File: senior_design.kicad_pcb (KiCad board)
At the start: 2 copper layers, 128.6 x 80.8 mm, 129 parts, among them J10 Conn_01x01_Pin, J11 Conn_01x01_Pin, J12 Conn_01x01_Pin, J13 Conn_ARM_JTAG_SWD_10, J2 Conn_01x03_Pin, J3 Conn_01x09_Socket, J4 USB_B_Micro, J5 Out_to_display, J6 AudioJack3, J7 SD_Card_Receptacle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

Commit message: Some fixes
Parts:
- removed C27: 1uF, Capacitor_SMD:C_0805_2012Metric
- C21, C22, L1, R41: moved to F.Cu
- C25, C26: value 0.1uF -> .1uF; moved to F.Cu
- C30, C8: moved to B.Cu
- C31: value 0.1uF -> 1uF; moved to B.Cu
- R38: value R -> 10k
- moved C31 36.9 mm to (231.6, 93.7), turned to 0 degrees
- moved C33 28.4 mm to (228.2, 77.5), turned to 90 degrees
- moved C28 26.9 mm to (207.2, 92.5), turned to 180 degrees
- moved C26 23.1 mm to (208.3, 97.0), turned to 180 degrees
- moved C34 15.5 mm to (218.1, 90.3), turned to 0 degrees
- moved C22 13.9 mm to (206.4, 81.7), turned to 0 degrees
- moved C32 12.9 mm to (229.4, 67.1), turned to 0 degrees
- moved R41 11.3 mm to (223.1, 66.2)
- moved C29 11.1 mm to (216.9, 87.7), turned to 0 degrees
- moved C30 10.8 mm to (218.0, 96.0), turned to 90 degrees
- moved C16 10.5 mm to (224.8, 56.5), turned to -90 degrees
- moved Y1 9.98 mm to (208.8, 78.2), turned to 0 degrees
- moved R38 9.40 mm to (208.8, 84.2), turned to 180 degrees
- moved D6 8.10 mm to (216.7, 79.7)
- moved L1 7.83 mm to (228.4, 62.0), turned to 90 degrees
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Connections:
- C23 pad 1: +1V5 -> CORE_VDD
- C24 pad 1: +1V5 -> CORE_VDD
- C25 pad 1: +1V5 -> +3.3V
- C26 pad 1: +1V5 -> +3.3V
- C30 pad 1: +3.3V -> GND
- C30 pad 2: GND -> CORE_VDD
- C31 pad 1: +3.3V -> CORE_VDD
- C34 pad 1: +3.3V -> Net-(U3-OSC_VDD)
- U3 pad 17: +1V5 -> CORE_VDD
- U3 pad 38: +1V5 -> CORE_VDD
- U3 pad 5: +1V5 -> Net-(U3-OSC_VDD)
- U3 pad 60: +1V5 -> CORE_VDD
- U3 pad 86: +1V5 -> CORE_VDD
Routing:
- net +1V5: track 56.3 -> 0.00 mm, vias 6 -> 0
- net CORE_VDD: track 0.00 -> 45.9 mm, vias 0 -> 6
- net GND: track 189.6 -> 218.0 mm, vias 73 -> 79
- net /Peripherals/X_0: track 24.3 -> 11.7 mm, vias 1 -> 0
- net Net-(D6-A): track 24.6 -> 13.9 mm, vias 0 -> 1
- net /Peripherals/X_1: track 20.1 -> 10.00 mm, vias 1 -> 0
- net Net-(U3-OSC_VDD): track 0.00 -> 6.78 mm, vias 0 -> 1
- net /Peripherals/LEDK: track 28.3 -> 34.5 mm
- net +3.3V: track 186.7 -> 181.6 mm
- net +5V: track 148.8 -> 152.4 mm, vias 4 -> 2
- net Net-(D7-A): track 14.6 -> 11.9 mm, vias 1 -> 0
- net /Peripherals/VSYNC: track 45.1 -> 43.8 mm
- net +24V: track 13.8 -> 14.7 mm
- net /Peripherals/PWM0: track 18.1 -> 17.6 mm

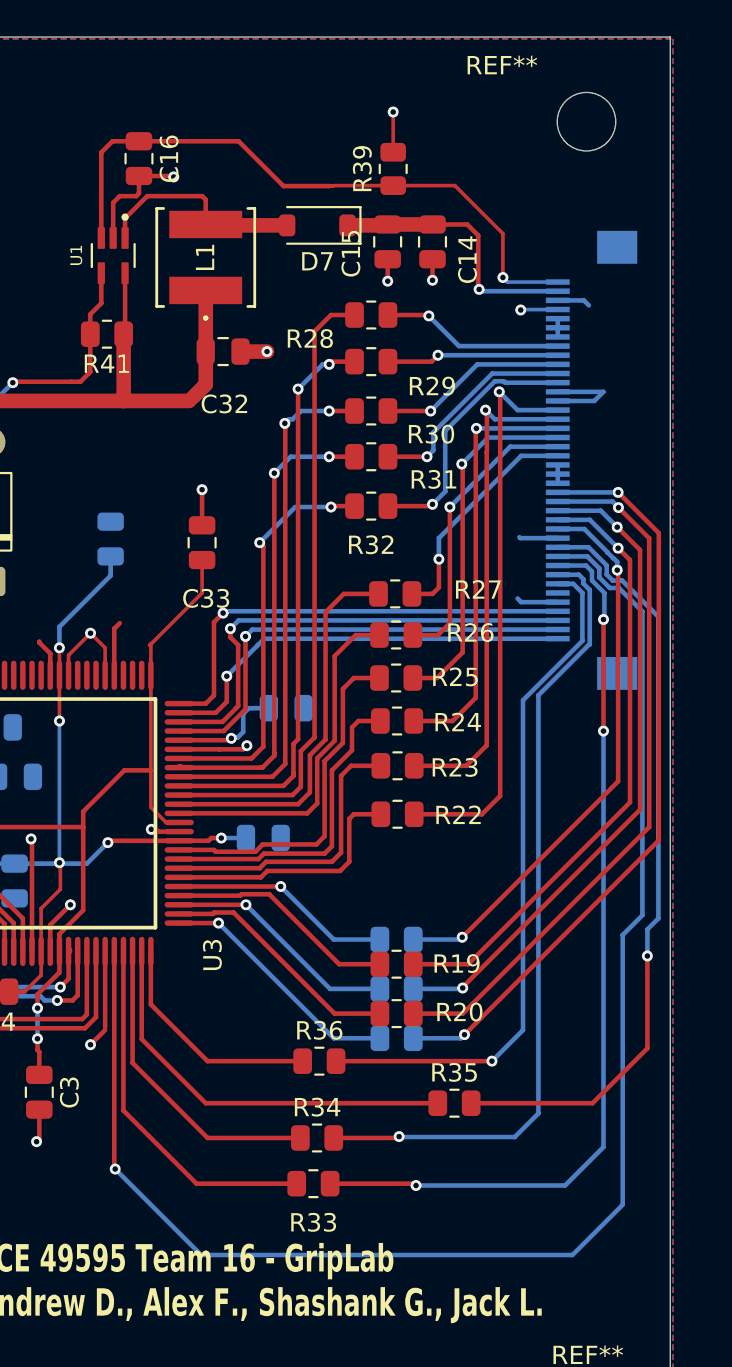
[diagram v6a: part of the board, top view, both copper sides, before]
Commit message: shortened data lines
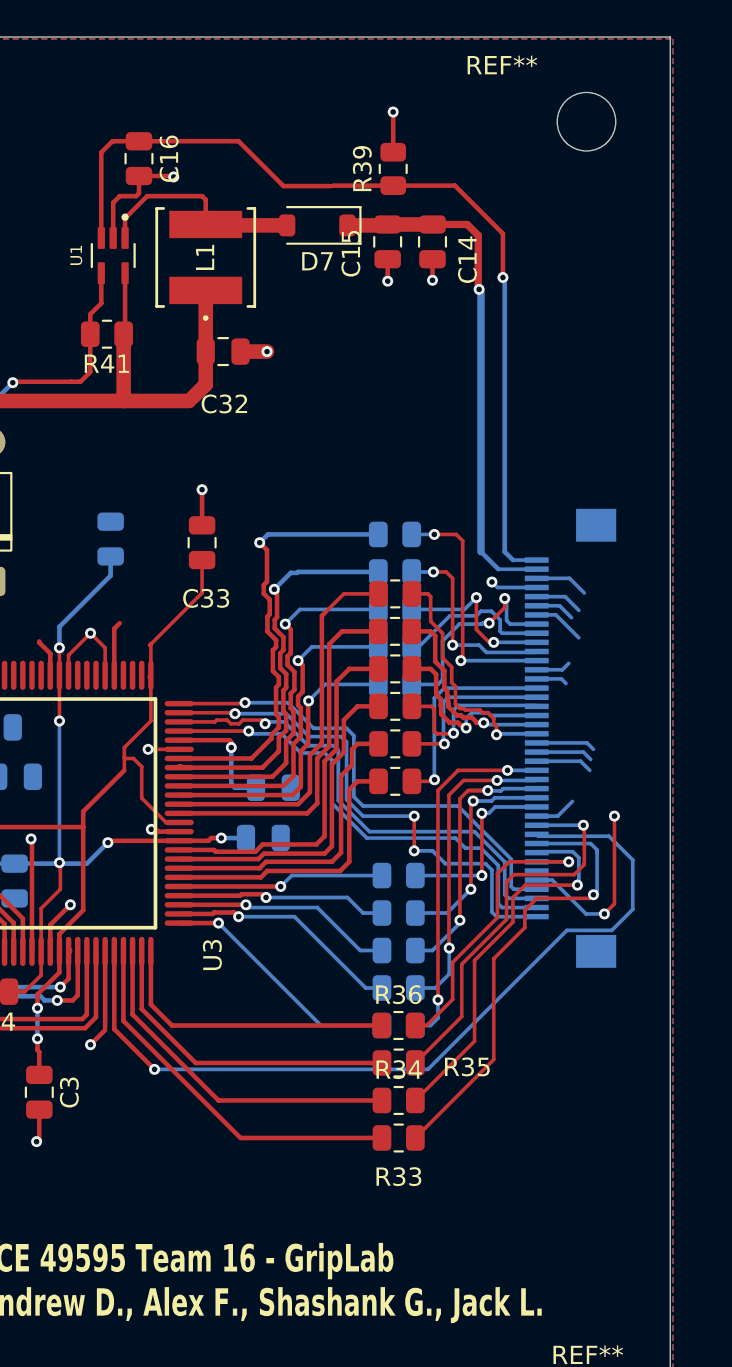
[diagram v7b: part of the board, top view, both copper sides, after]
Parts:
- R19, R20, R28, R29, R30, R31, R32: moved to B.Cu
- moved R28 20.2 mm to (238.8, 85.3)
- moved R29 15.7 mm to (238.8, 83.2)
- moved J5 15.2 mm to (248.4, 88.2)
- moved R30 10.9 mm to (238.8, 81.2)
- moved R31 6.43 mm to (238.8, 79.2)
- moved R33 5.29 mm to (239.0, 110.1)
- moved R34 4.91 mm to (239.0, 108.0)
- moved R36 4.74 mm to (239.0, 104.0)
- moved C18 4.41 mm to (232.2, 91.0)
- moved R35 3.76 mm to (239.0, 106.0)
- moved R21 3.50 mm to (239.0, 95.8)
- moved R19 2.80 mm to (239.0, 97.8)
- moved R18 2.10 mm to (239.0, 99.8)
- moved R32 2.02 mm to (238.8, 77.1)
- moved R22 1.80 mm to (238.8, 90.6)
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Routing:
- net /Peripherals/ON/OFF: track 81.8 -> 45.7 mm
- net /Peripherals/HSYNC: track 49.6 -> 25.0 mm, vias 3 -> 1
- net /Peripherals/VSYNC: track 43.8 -> 21.1 mm
- net /Peripherals/B4: track 39.0 -> 17.1 mm, vias 1 -> 2
- net /Peripherals/B6: track 33.7 -> 12.0 mm, vias 1 -> 2
- net /Peripherals/B3: track 41.2 -> 19.7 mm
- net /Peripherals/DE: track 37.9 -> 16.5 mm
- net /Peripherals/B5: track 36.1 -> 15.3 mm
- net /Peripherals/PIXCLK: track 42.1 -> 21.3 mm
- net /Peripherals/B7: track 30.8 -> 10.4 mm
- net GND: track 218.0 -> 238.5 mm, vias 79 -> 81
- net /Peripherals/G2: track 30.8 -> 11.6 mm
- net Net-(U3-PDAT11): track 34.6 -> 15.9 mm, vias 0 -> 1
- net /Peripherals/G3: track 27.0 -> 9.30 mm
- net /Peripherals/LEDK: track 34.5 -> 48.4 mm
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
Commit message: changed spis
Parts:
- added R16: 1M, Resistor_SMD:R_0805_2012Metric, F.Cu at (192.6, 53.9)
- moved J3 44.4 mm to (200.2, 63.8), turned to 90 degrees
- moved U9 14.8 mm to (177.1, 100.0)
- moved J7 14.1 mm to (176.9, 117.8)
- moved C10 9.76 mm to (213.4, 73.3)
- moved L1 6.42 mm to (234.2, 64.9)
- moved R39 6.42 mm to (244.4, 60.1)
- moved C14 6.42 mm to (246.6, 64.0)
- moved U1 6.42 mm to (229.1, 64.8)
- moved C16 6.42 mm to (230.5, 59.5)
- moved C32 6.42 mm to (235.1, 70.0)
- moved C15 6.42 mm to (244.1, 64.0)
- moved D7 6.42 mm to (240.2, 63.1)
- moved R41 6.42 mm to (228.8, 69.1)
- moved C7 4.54 mm to (195.2, 70.6)
- moved D5 3.69 mm to (195.8, 67.0)
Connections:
- net ADC_IN1 renamed /Hall Effect/ADC_IN1
- net ADC_IN2 renamed /Hall Effect/ADC_IN2
- net AUDIO_IN renamed /Audio/AUDIO_IN
- net I2C1_SCL renamed /MCU/I2C1_SDA
- net I2C1_SDA renamed /MCU/I2C1_SCL
- J3 pad 3: /MCU/SPI4_SCK -> /MCU/CS2
- J3 pad 4: /MCU/SPI4_MISO -> /MCU/SCK2
- J3 pad 5: /MCU/SPI4_MOSI -> /MCU/MOSI2
- J3 pad 6: /MCU/SPI4_CS -> /MCU/MISO2
- J4 pad 6: GND -> Net-(J4-Shield)
- J7 pad 1: SPI_SSD -> /MCU/SPI4_CS
- J7 pad 2: SPI_MOSI -> /MCU/SPI4_MISO
- J7 pad 5: SPI_SCLK -> /MCU/SPI4_MOSI
- J7 pad 7: SPI_MISO -> /MCU/SPI4_SCK
- U6 pad 34: /MCU/SPI4_WAIT -> unconnected-(U6-PE9-Pad34)
- U6 pad 35: /MCU/SPI4_RST -> unconnected-(U6-PE10-Pad35)
- U6 pad 40: /MCU/SPI4_INT -> unconnected-(U6-PE15-Pad40)
- U6 pad 72: unconnected-(U6-PA10-Pad72) -> /MCU/SPI4_WAIT
- U6 pad 73: unconnected-(U6-PA11-Pad73) -> /MCU/SPI4_RST
- U6 pad 74: unconnected-(U6-PA12-Pad74) -> /MCU/SPI4_INT
- U6 pad 80: SPI_SSD -> /MCU/CS2
- U6 pad 81: SPI_SCLK -> /MCU/SCK2
- U6 pad 82: SPI_MISO -> /MCU/MISO2
- U6 pad 83: SPI_MOSI -> /MCU/MOSI2
- U9 pad 1: SPI_MISO -> /MCU/SPI4_SCK
- U9 pad 3: SPI_SSD -> /MCU/SPI4_CS
- U9 pad 4: SPI_SCLK -> /MCU/SPI4_MOSI
- U9 pad 6: SPI_MOSI -> /MCU/SPI4_MISO
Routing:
- net SPI_MISO: track 62.8 -> 0.00 mm, vias 3 -> 0
- net SPI_SCLK: track 62.8 -> 0.00 mm, vias 2 -> 0
- net +5V: track 152.4 -> 90.2 mm, vias 2 -> 0
- net SPI_SSD: track 61.3 -> 0.00 mm, vias 2 -> 0
- net SPI_MOSI: track 52.3 -> 0.00 mm, vias 4 -> 0
- net /MCU/MISO2: track 0.00 -> 23.5 mm, vias 0 -> 1
- net /MCU/MOSI2: track 0.00 -> 22.6 mm, vias 0 -> 1
- net /MCU/SCK2: track 0.00 -> 20.1 mm, vias 0 -> 1
- net /MCU/SPI4_SCK: track 23.7 -> 39.6 mm, vias 0 -> 1
- net /MCU/CS2: track 0.00 -> 15.9 mm
- net GND: track 238.5 -> 223.7 mm
- net /MCU/SPI4_INT: track 37.7 -> 24.6 mm, vias 0 -> 1
- net Net-(J4-Shield): track 0.00 -> 12.5 mm
- net +3.3V: track 183.0 -> 171.0 mm, vias 12 -> 6
- net /MCU/SPI4_WAIT: track 33.0 -> 23.7 mm, vias 2 -> 1
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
